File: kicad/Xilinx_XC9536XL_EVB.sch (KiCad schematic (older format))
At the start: 56 parts, among them IC1 ATTINY2313-P, P1 CONN_7X2, P2 CONN_2, P3 CONN_3X2, P4 CONN_5, P5 CONN_5, P6 CONN_12, P7 CONN_6, P8 CONN_8, SW1 SW_PUSH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

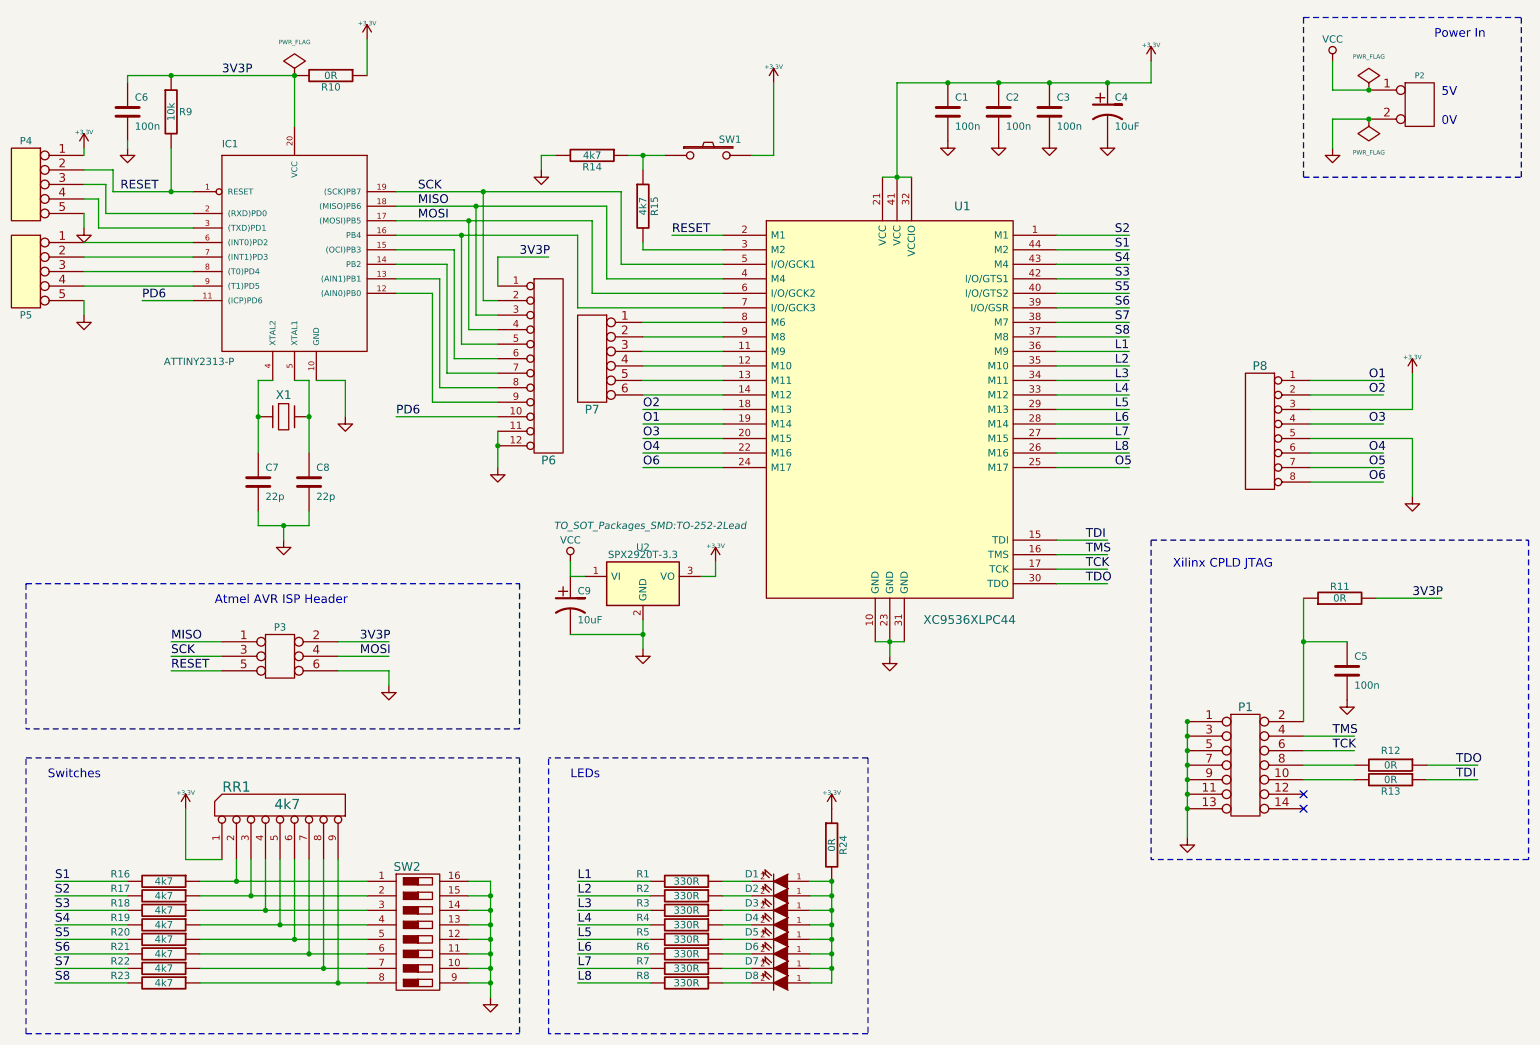
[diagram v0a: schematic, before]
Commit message: updated pcb with new footprints
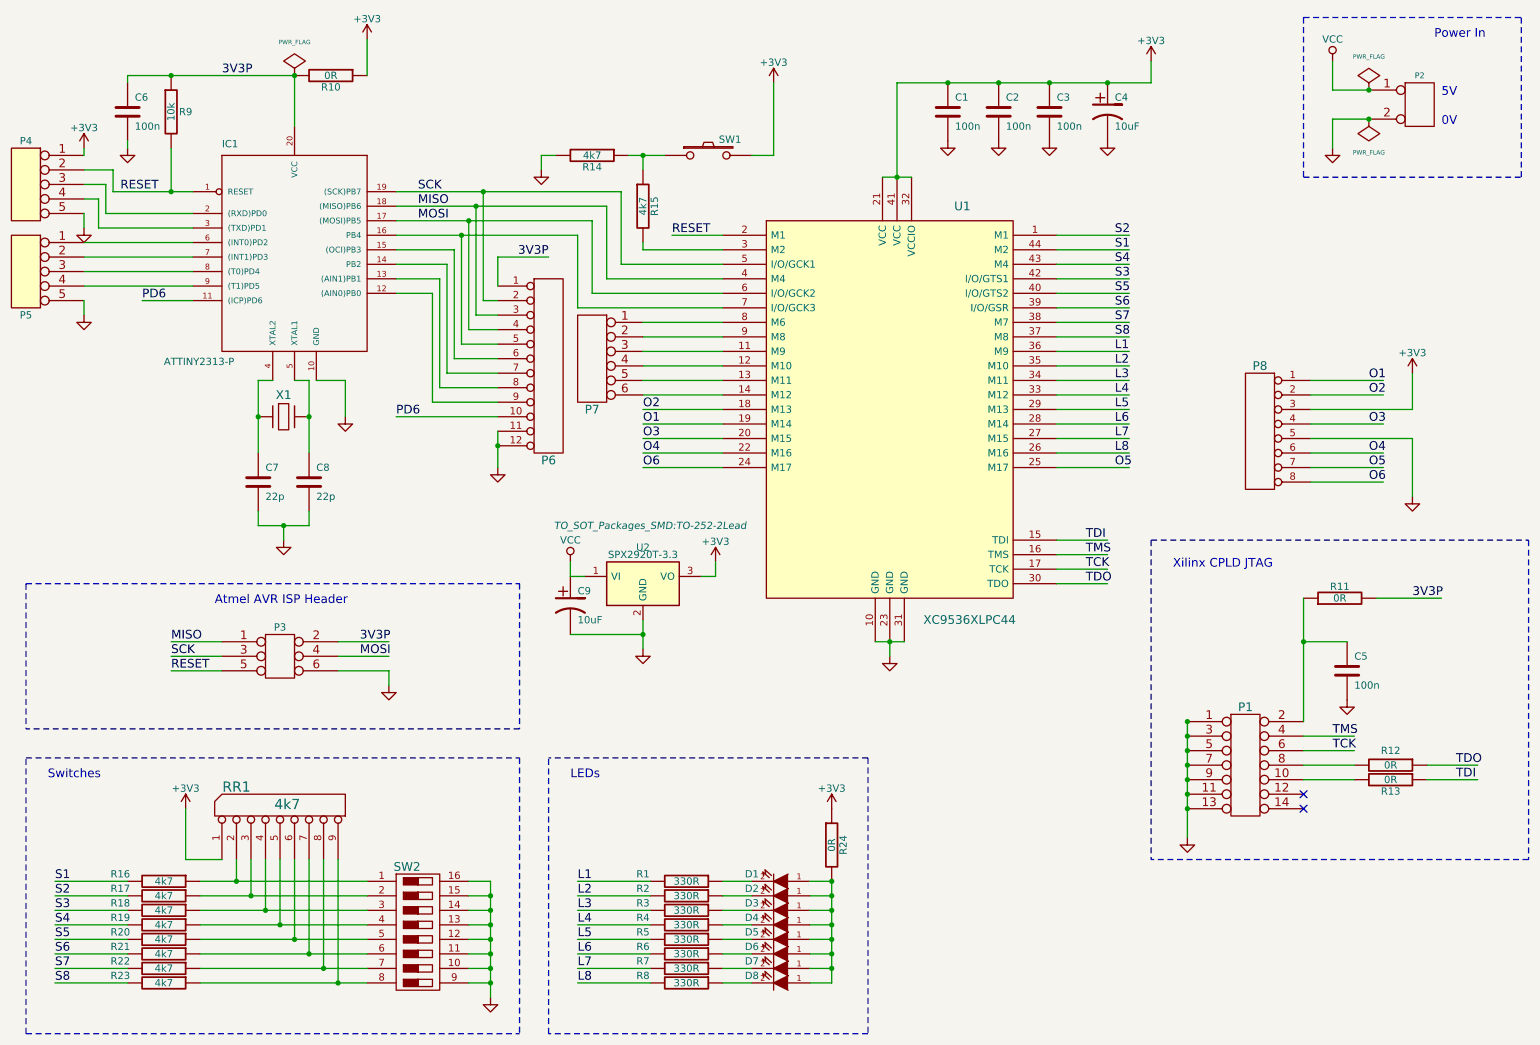
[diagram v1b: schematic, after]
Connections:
- net labels added: +3V3
- net labels removed: +3.3V

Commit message: automatic switch to kicad 5 format
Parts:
- C1, C2, C3, C5, C6, C7, C8: symbol C-RESCUE-Xilinx_XC9536XL_EVB -> Xilinx_XC9536XL_EVB-rescue:C-RESCUE-Xilinx_XC9536XL_EVB
- C4, C9: symbol CP1-RESCUE-Xilinx_XC9536XL_EVB -> Xilinx_XC9536XL_EVB-rescue:CP1-RESCUE-Xilinx_XC9536XL_EVB
- D1, D2, D3, D4, D5, D6, D7, D8: symbol LED-RESCUE-Xilinx_XC9536XL_EVB -> Xilinx_XC9536XL_EVB-rescue:LED-RESCUE-Xilinx_XC9536XL_EVB
- IC1: symbol ATTINY2313-P_old -> Xilinx_XC9536XL_EVB-rescue:ATTINY2313-P_old
- P1: symbol CONN_7X2 -> Xilinx_XC9536XL_EVB-rescue:CONN_7X2
- P2: symbol CONN_2 -> Xilinx_XC9536XL_EVB-rescue:CONN_2
- P3: symbol CONN_3X2 -> Xilinx_XC9536XL_EVB-rescue:CONN_3X2
- P4, P5: symbol CONN_5 -> Xilinx_XC9536XL_EVB-rescue:CONN_5
- P6: symbol CONN_12 -> Xilinx_XC9536XL_EVB-rescue:CONN_12
- P7: symbol CONN_6 -> Xilinx_XC9536XL_EVB-rescue:CONN_6
- P8: symbol CONN_8 -> Xilinx_XC9536XL_EVB-rescue:CONN_8
- R1, R10, R11, R12, R13, R14, R15, R16, R17, R18, R19, R2, R20, R21, R22, R23, R24, R3, R4, R5, R6, R7, R8, R9: symbol R-RESCUE-Xilinx_XC9536XL_EVB -> Xilinx_XC9536XL_EVB-rescue:R-RESCUE-Xilinx_XC9536XL_EVB
- RR1: symbol RR8 -> Xilinx_XC9536XL_EVB-rescue:RR8
- SW1: symbol SW_PUSH -> Xilinx_XC9536XL_EVB-rescue:SW_PUSH
- SW2: symbol SW_DIP_8 -> Xilinx_XC9536XL_EVB-rescue:SW_DIP_8
- U1: symbol XC9536PC44 -> Xilinx_XC9536XL_EVB-rescue:XC9536PC44
- U2: symbol SPX2920T-3.3 -> Xilinx_XC9536XL_EVB-rescue:SPX2920T-3.3
- X1: symbol XTAL -> Xilinx_XC9536XL_EVB-rescue:XTAL
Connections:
- wire segments 213 -> 259
